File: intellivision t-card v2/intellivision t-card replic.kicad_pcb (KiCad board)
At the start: 2 copper layers, 143 x 165.9 mm, 75 parts, among them J1 2x22 card edge connector, SW1 SW_DIP_x08, SW2 SW_DIP_x08, SW3 SW_DIP_x08, SW4 SW_DIP_x08, U1 74LS374, U10 74LS00, U11 74LS85, U12 74LS51, U13 74LS00, U14 74LS85, U15 74LS51, U16 74LS00, U17 74LS85, U18 2732, U19 2732, U2 74LS374, U20 2732, U21 2732, U22 2732, U23 2732, U24 2732, U25 2732, U3 74LS42, U5 74LS08, U6 74LS51, U7 74LS00, U8 74LS85, U9 74LS51

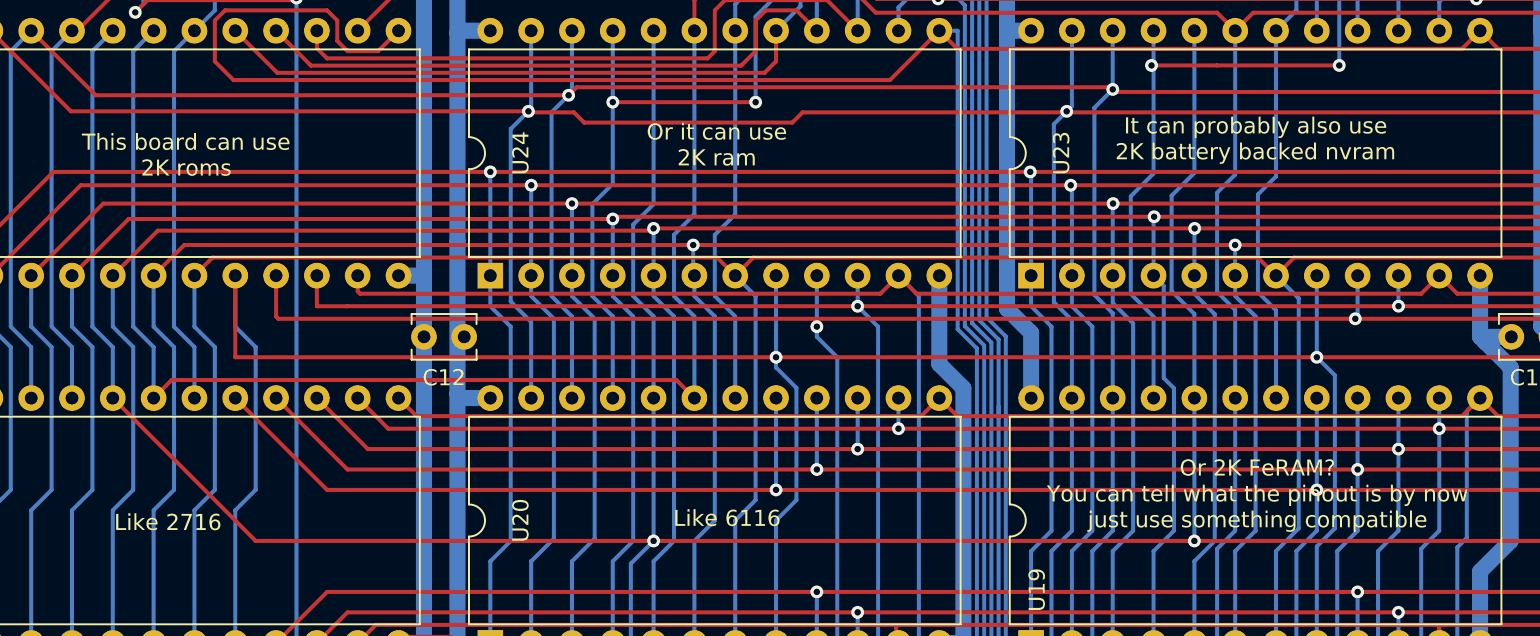
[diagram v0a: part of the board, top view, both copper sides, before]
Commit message: fixed silk about 2k/4k roms
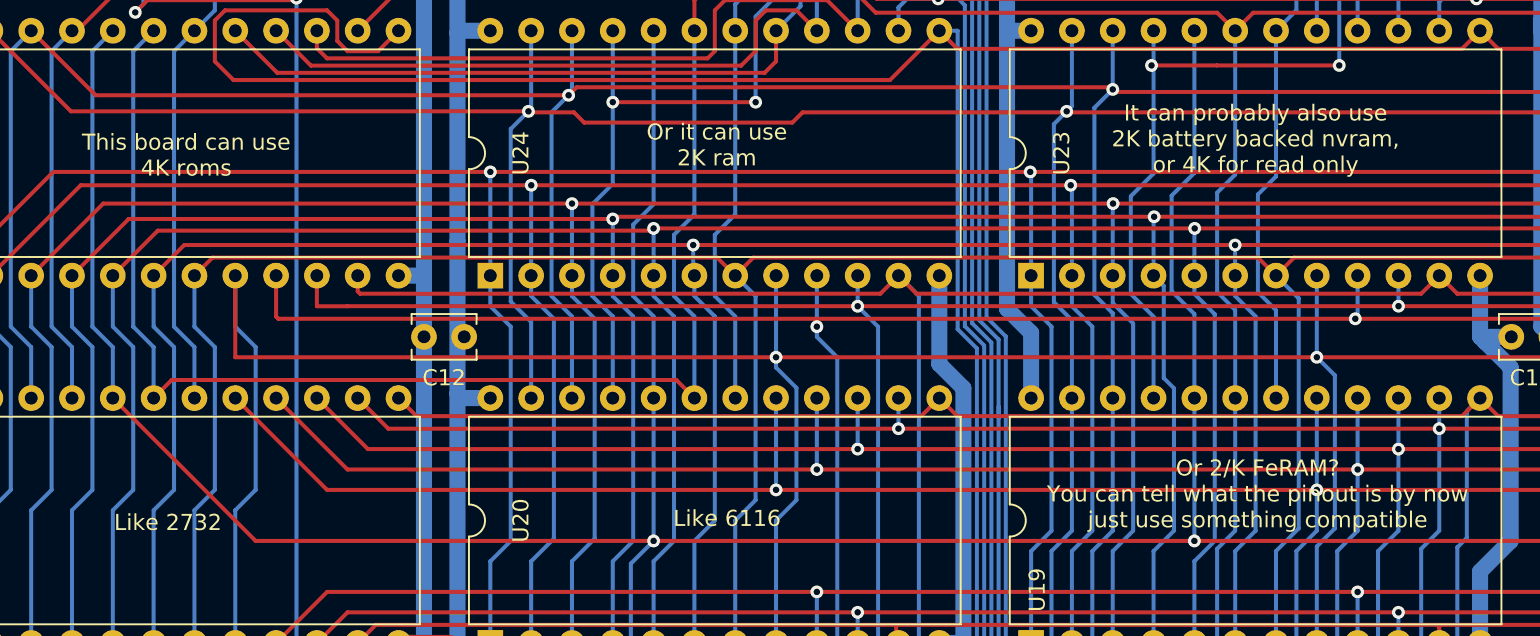
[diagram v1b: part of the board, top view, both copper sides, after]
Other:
- board text added: "It can probably also use 2K battery backed nvram, or 4K for read only"
- board text added: "Like 2732"
- board text added: "Or 2/K FeRAM? You can tell what the pinout is by now just use something compatible"
- board text added: "This board can use 4K roms"
- board text removed: "It can probably also use 2K battery backed nvram"
- board text removed: "Like 2716"
- board text removed: "Or 2K FeRAM? You can tell what the pinout is by now just use something compatible"
- board text removed: "This board can use 2K roms"
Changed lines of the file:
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@@
     (effects (font (size 1.3 1.3) (thickness 0.2)) (justify left))
   )
-  (gr_text "Like 2716" (at 67.564 101.092) (layer "F.SilkS")
+  (gr_text "Like 2732" (at 67.564 101.092) (layer "F.SilkS")
     (effects (font (size 1 1) (thickness 0.15)))
   )
@@
     (effects (font (size 1.3 1.3) (thickness 0.2)) (justify left))
   )
-  (gr_text "Or 2K FeRAM? \nYou can tell what the pinout is by now\njust use something compatible" (at 135.382 99.314) (layer "F.SilkS")
+  (gr_text "Or 2/K FeRAM? \nYou can tell what the pinout is by now\njust use something compatible" (at 135.382 99.314) (layer "F.SilkS")
     (effects (font (size 1 1) (thickness 0.15)))
   )
@@
     (effects (font (size 1.3 1.3) (thickness 0.2)) (justify left))
   )
-  (gr_text "It can probably also use \n2K battery backed nvram" (at 135.255 77.216) (layer "F.SilkS")
+  (gr_text "It can probably also use \n2K battery backed nvram, \nor 4K for read only" (at 135.255 77.216) (layer "F.SilkS")
     (effects (font (size 1 1) (thickness 0.15)))
   )
@@
     (effects (font (size 1.3 1.3) (thickness 0.2)) (justify left))
   )
-  (gr_text "This board can use\n2K roms" (at 68.707 78.232) (layer "F.SilkS")
+  (gr_text "This board can use\n4K roms" (at 68.707 78.232) (layer "F.SilkS")
     (effects (font (size 1 1) (thickness 0.15)))
   )
